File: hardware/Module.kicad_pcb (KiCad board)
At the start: 2 copper layers, 57.5 x 109.2 mm, 32 parts, among them J1 CV_IN_1, J10 GATE_OUT_2, J11 AUDIO_IN_L, J12 AUDIO_IN_R, J13 AUDIO_OUT_L, J14 AUDIO_OUT_R, J15 POWER, J2 CV_IN_2, J3 CV_IN_3, J4 CV_IN_4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

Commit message: Fix power connector direction
Signed-off-by: Petr Horacek <petr@zlosynth.com>
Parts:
- moved J15 11.3 mm to (99.1, 112.6), turned to 180 degrees
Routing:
- net VCC: track 94.6 -> 111.9 mm
- net VEE: track 73.6 -> 83.1 mm
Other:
- board text added: "-12V"
- board text added: "Power"
- board text added: "RED"
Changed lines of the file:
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@@
   (net 57 "CV_IN_3")
   (footprint "Connector_PinHeader_2.54mm:PinHeader_2x05_P2.54mm_Vertical" (layer "F.Cu")
-    (at 96.15 101.68)
+    (at 99.11 112.62 180)
     (descr "Through hole straight pin header, 2x05, 2.54mm pitch, double rows")
     (tags "Through hole pin header THT 2x05 2.54mm double row")
@@
     (property "ki_keywords" "connector")
     (attr through_hole)
-    (fp_text reference "J15" (at 1.27 -2.33) (layer "F.SilkS")
+    (fp_text reference "J15" (at 1.27 -2.33) (layer "F.SilkS") hide
         (effects (font (size 1 1) (thickness 0.15)))
     )
@@
     (fp_line (start 3.81 11.43) (end -1.27 11.43)
       (stroke (width 0.1) (type solid)) (layer "F.Fab"))
-    (pad "1" thru_hole rect (at 0 0) (size 1.7 1.7) (drill 1) (layers "*.Cu" "*.Mask")
+    (pad "1" thru_hole rect (at 0 0 180) (size 1.7 1.7) (drill 1) (layers "*.Cu" "*.Mask")
       (net 1 "VCC") (pinfunction "Pin_1") (pintype "passive"))
-    (pad "2" thru_hole oval (at 2.54 0) (size 1.7 1.7) (drill 1) (layers "*.Cu" "*.Mask")
+    (pad "2" thru_hole oval (at 2.54 0 180) (size 1.7 1.7) (drill 1) (layers "*.Cu" "*.Mask")
       (net 1 "VCC") (pinfunction "Pin_2") (pintype "passive"))
-    (pad "3" thru_hole oval (at 0 2.54) (size 1.7 1.7) (drill 1) (layers "*.Cu" "*.Mask")
+    (pad "3" thru_hole oval (at 0 2.54 180) (size 1.7 1.7) (drill 1) (layers "*.Cu" "*.Mask")
       (net 2 "GND") (pinfunction "Pin_3") (pintype "passive"))
-    (pad "4" thru_hole oval (at 2.54 2.54) (size 1.7 1.7) (drill 1) (layers "*.Cu" "*.Mask")
+    (pad "4" thru_hole oval (at 2.54 2.54 180) (size 1.7 1.7) (drill 1) (layers "*.Cu" "*.Mask")
       (net 2 "GND") (pinfunction "Pin_4") (pintype "passive"))
-    (pad "5" thru_hole oval (at 0 5.08) (size 1.7 1.7) (drill 1) (layers "*.Cu" "*.Mask")
+    (pad "5" thru_hole oval (at 0 5.08 180) (size 1.7 1.7) (drill 1) (layers "*.Cu" "*.Mask")
       (net 2 "GND") (pinfunction "Pin_5") (pintype "passive"))
-    (pad "6" thru_hole oval (at 2.54 5.08) (size 1.7 1.7) (drill 1) (layers "*.Cu" "*.Mask")
+    (pad "6" thru_hole oval (at 2.54 5.08 180) (size 1.7 1.7) (drill 1) (layers "*.Cu" "*.Mask")
       (net 2 "GND") (pinfunction "Pin_6") (pintype "passive"))
-    (pad "7" thru_hole oval (at 0 7.62) (size 1.7 1.7) (drill 1) (layers "*.Cu" "*.Mask")
+    (pad "7" thru_hole oval (at 0 7.62 180) (size 1.7 1.7) (drill 1) (layers "*.Cu" "*.Mask")
       (net 2 "GND") (pinfunction "Pin_7") (pintype "passive"))
-    (pad "8" thru_hole oval (at 2.54 7.62) (size 1.7 1.7) (drill 1) (layers "*.Cu" "*.Mask")
+    (pad "8" thru_hole oval (at 2.54 7.62 180) (size 1.7 1.7) (drill 1) (layers "*.Cu" "*.Mask")
       (net 2 "GND") (pinfunction "Pin_8") (pintype "passive"))
-    (pad "9" thru_hole oval (at 0 10.16) (size 1.7 1.7) (drill 1) (layers "*.Cu" "*.Mask")
+    (pad "9" thru_hole oval (at 0 10.16 180) (size 1.7 1.7) (drill 1) (layers "*.Cu" "*.Mask")
       (net 3 "VEE") (pinfunction "Pin_9") (pintype "passive"))
-    (pad "10" thru_hole oval (at 2.54 10.16) (size 1.7 1.7) (drill 1) (layers "*.Cu" "*.Mask")
+    (pad "10" thru_hole oval (at 2.54 10.16 180) (size 1.7 1.7) (drill 1) (layers "*.Cu" "*.Mask")
       (net 3 "VEE") (pinfunction "Pin_10") (pintype "passive"))
     (model "${KICAD6_3DMODEL_DIR}/Connector_PinHeader_2.54mm.3dshapes/PinHeader_2x05_P2.54mm_Vertical.wrl"
@@
     )
   )
+  (gr_rect (start 93.485 103.68) (end 101.91 100.48)
+    (stroke (width 0.15) (type solid)) (fill solid) (layer "F.SilkS"))
   (gr_circle (center 52.37 158.88584) (end 53.77 159.43584)
     (stroke (width 0.1) (type default)) (fill none) (layer "Edge.Cuts"))
@@
     (effects (font (size 1 1) (thickness 0.15)) (justify left bottom))
   )
-  (segment (start 62.11 138.84172) (end 62.11 144.992258) (width 1) (layer "F.Cu") (net 1))
+  (gr_text "-12V" (at 95.765 98.75 180) (layer "F.SilkS")
+    (effects (font (size 1 1) (thickness 0.15)) (justify bottom))
+  )
+  (gr_text "Power" (at 102.29 109.82 90) (layer "F.SilkS")
+    (effects (font (size 1 1) (thickness 0.15)) (justify left bottom))
+  )
+  (gr_text "RED" (at 99.985 98.75 180) (layer "F.SilkS")
+    (effects (font (size 1 1) (thickness 0.15)) (justify bottom))
+  )
+  (segment (start 85.826472 106.796472) (end 91.712944 100.91) (width 1) (layer "F.Cu") (net 1))
+  (segment (start 99.11 112.62) (end 96.57 112.62) (width 1) (layer "F.Cu") (net 1))
   (segment (start 60.48 146.622258) (end 60.48 147.847742) (width 1) (layer "F.Cu") (net 1))
   (segment (start 60.48 147.847742) (end 62.167258 149.535) (width 1) (layer "F.Cu") (net 1))
-  (segment (start 55.4225 137.1075) (end 60.37578 137.1075) (width 1) (layer "F.Cu") (net 1))
-  (segment (start 62.167258 149.535) (end 72.147944 149.535) (width 1) (layer "F.Cu") (net 1))
-  (segment (start 53.77 138.76) (end 55.4225 137.1075) (width 1) (layer "F.Cu") (net 1))
+  (segment (start 100.66 111.07) (end 99.11 112.62) (width 1) (layer "F.Cu") (net 1))
   (segment (start 60.37578 137.1075) (end 62.11 138.84172) (width 1) (layer "F.Cu") (net 1))
+  (segment (start 91.712944 100.91) (end 99.82 100.91) (width 1) (layer "F.Cu") (net 1))
+  (segment (start 53.77 138.76) (end 55.4225 137.1075) (width 1) (layer "F.Cu") (net 1))
+  (segment (start 85.826472 123.036472) (end 85.826472 106.796472) (width 1) (layer "F.Cu") (net 1))
+  (segment (start 62.167258 149.535) (end 72.147944 149.535) (width 1) (layer "F.Cu") (net 1))
+  (segment (start 72.147944 149.535) (end 74.11 147.572944) (width 1) (layer "F.Cu") (net 1))
+  (segment (start 62.11 138.84172) (end 62.11 144.992258) (width 1) (layer "F.Cu") (net 1))
   (segment (start 74.11 134.752944) (end 85.826472 123.036472) (width 1) (layer "F.Cu") (net 1))
-  (segment (start 74.11 147.572944) (end 74.11 134.752944) (width 1) (layer "F.Cu") (net 1))
+  (segment (start 99.82 100.91) (end 100.66 101.75) (width 1) (layer "F.Cu") (net 1))
+  (segment (start 100.66 101.75) (end 100.66 111.07) (width 1) (layer "F.Cu") (net 1))
   (segment (start 62.11 144.992258) (end 60.48 146.622258) (width 1) (layer "F.Cu") (net 1))
-  (segment (start 85.826472 107.803528) (end 91.95 101.68) (width 1) (layer "F.Cu") (net 1))
-  (segment (start 72.147944 149.535) (end 74.11 147.572944) (width 1) (layer "F.Cu") (net 1))
-  (segment (start 85.826472 123.036472) (end 85.826472 107.803528) (width 1) (layer "F.Cu") (net 1))
-  (segment (start 98.69 101.68) (end 96.15 101.68) (width 1) (layer "F.Cu") (net 1))
-  (segment (start 91.95 101.68) (end 96.15 101.68) (width 1) (layer "F.Cu") (net 1))
-  (segment (start 91.29 111.84) (end 87.03 116.1) (width 1) (layer "F.Cu") (net 3))
-  (segment (start 98.69 111.84) (end 91.29 111.84) (width 1) (layer "F.Cu") (net 3))
+  (segment (start 74.11 147.572944) (end 74.11 134.752944) (width 1) (layer "F.Cu") (net 1))
+  (segment (start 55.4225 137.1075) (end 60.37578 137.1075) (width 1) (layer "F.Cu") (net 1))
+  (segment (start 91.86 102.46) (end 99.11 102.46) (width 1) (layer "F.Cu") (net 3))
   (segment (start 55.585 150.735) (end 53.77 148.92) (width 1) (layer "F.Cu") (net 3))
   (segment (start 87.026472 123.533528) (end 75.31 135.25) (width 1) (layer "F.Cu") (net 3))
   (segment (start 87.03 116.1) (end 87.026472 116.1) (width 1) (layer "F.Cu") (net 3))
+  (segment (start 87.026472 116.1) (end 87.026472 107.293528) (width 1) (layer "F.Cu") (net 3))
   (segment (start 87.026472 116.1) (end 87.026472 123.533528) (width 1) (layer "F.Cu") (net 3))
   (segment (start 75.31 148.07) (end 72.645 150.735) (width 1) (layer "F.Cu") (net 3))
   (segment (start 72.645 150.735) (end 55.585 150.735) (width 1) (layer "F.Cu") (net 3))
+  (segment (start 87.026472 107.293528) (end 91.86 102.46) (width 1) (layer "F.Cu") (net 3))
   (segment (start 75.31 135.25) (end 75.31 148.07) (width 1) (layer "F.Cu") (net 3))
   (segment (start 96.445 76.1) (end 94.86 76.1) (width 0.5) (layer "F.Cu") (net 6))

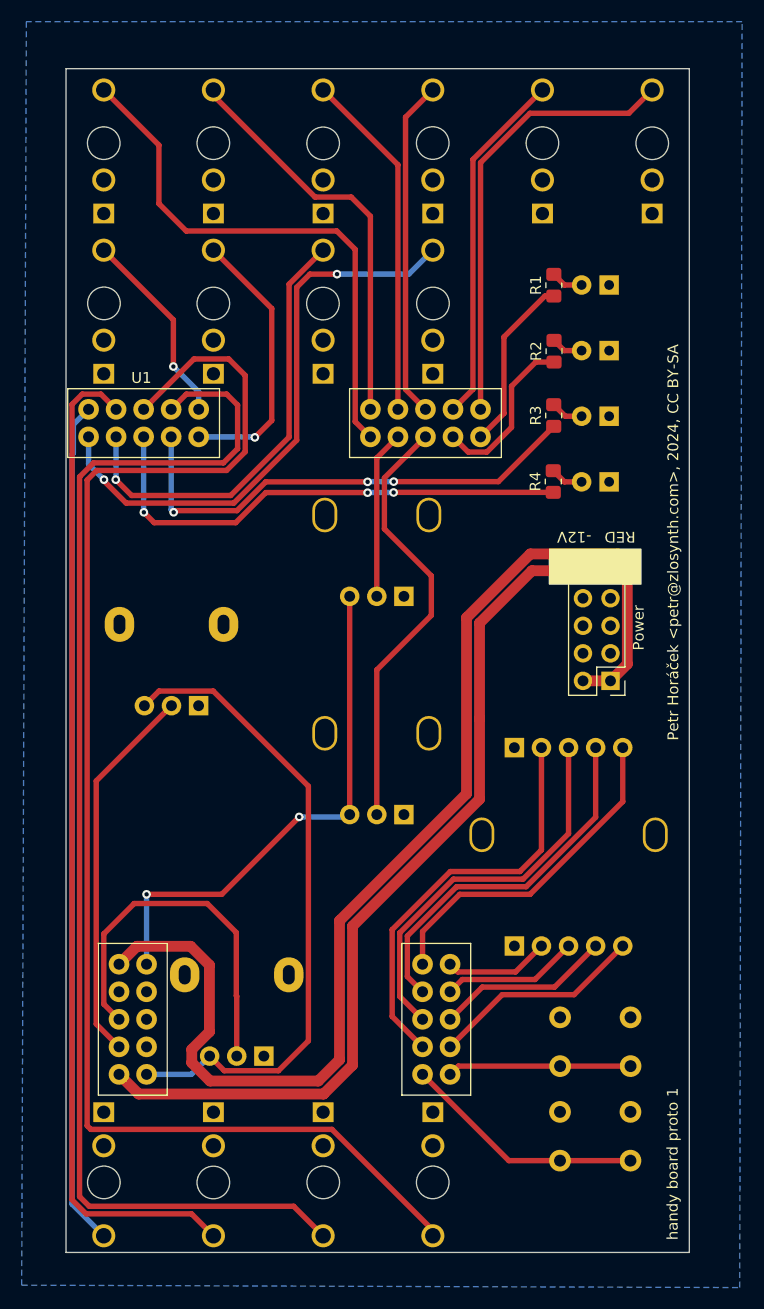
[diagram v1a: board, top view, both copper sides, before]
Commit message: Fix LED daisy connection
Signed-off-by: Petr Horacek <petr@zlosynth.com>
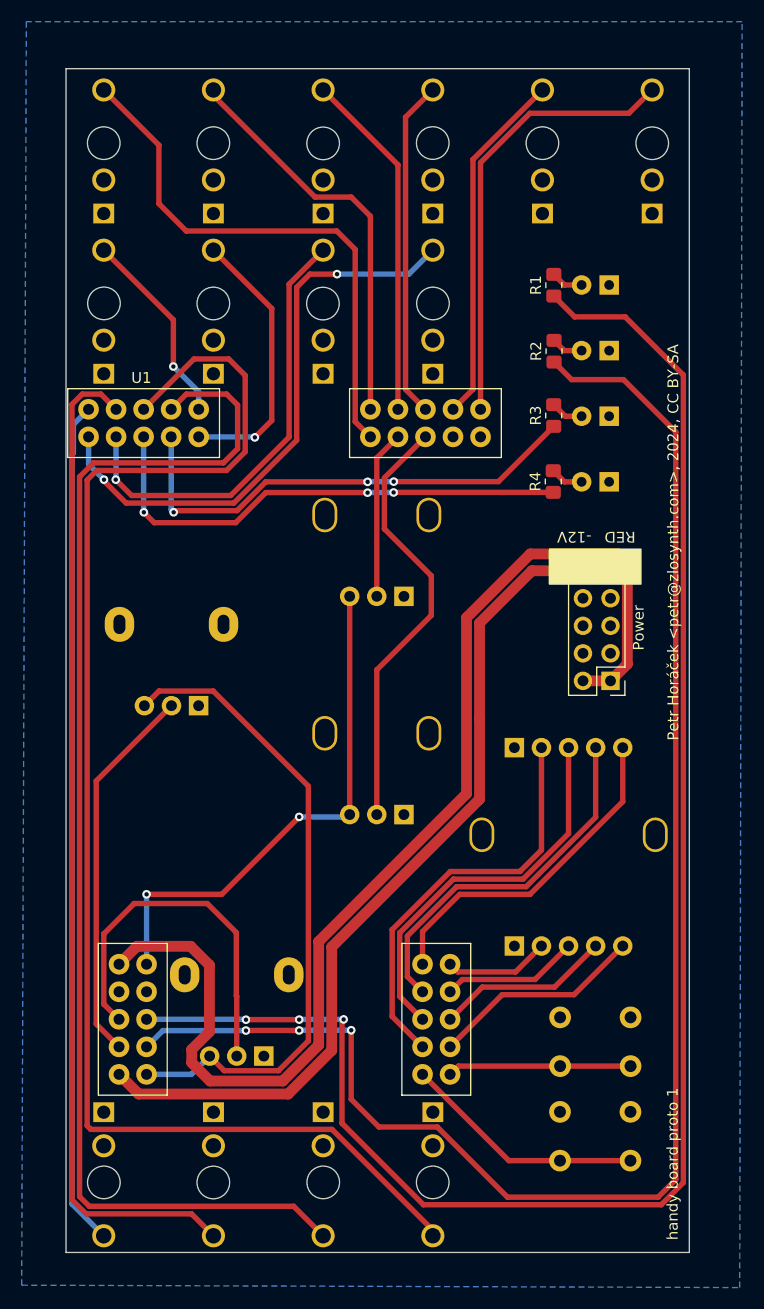
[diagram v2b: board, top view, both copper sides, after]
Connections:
- U1 pad A8: unconnected-(U1-USB_DM-PadA8) -> LED_1
- U1 pad A9: unconnected-(U1-USB_DP-PadA9) -> LED_2
- U1 pad C6: LED_1 -> unconnected-(U1-CV5-PadC6)
- U1 pad C7: LED_2 -> unconnected-(U1-CV6-PadC7)
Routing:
- net LED_1: track 16.3 -> 152.8 mm, vias 0 -> 3
- net LED_2: track 15.6 -> 143.1 mm, vias 0 -> 3
- net VCC: track 111.9 -> 109.9 mm
- net VEE: track 83.1 -> 81.2 mm
